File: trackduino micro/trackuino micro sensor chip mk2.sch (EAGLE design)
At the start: 39 parts, among them IC2 74AHC1G125DBV, SW1 SPST_TACT-KMR2, U1 ATMEGA168MLF, Y1 16MHZ

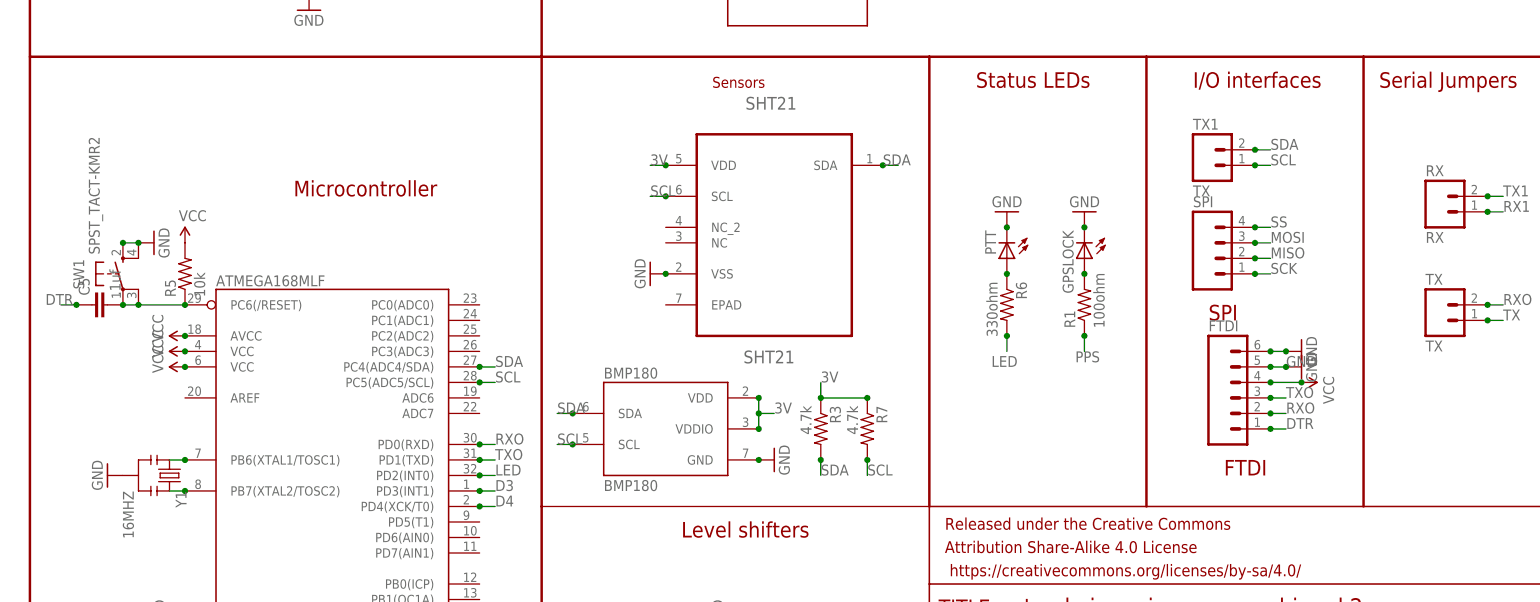
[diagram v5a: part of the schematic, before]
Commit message: Removed Reset Switch
removed reset switch from chip version and added a separate reset line
for ICSP / FTDI programming
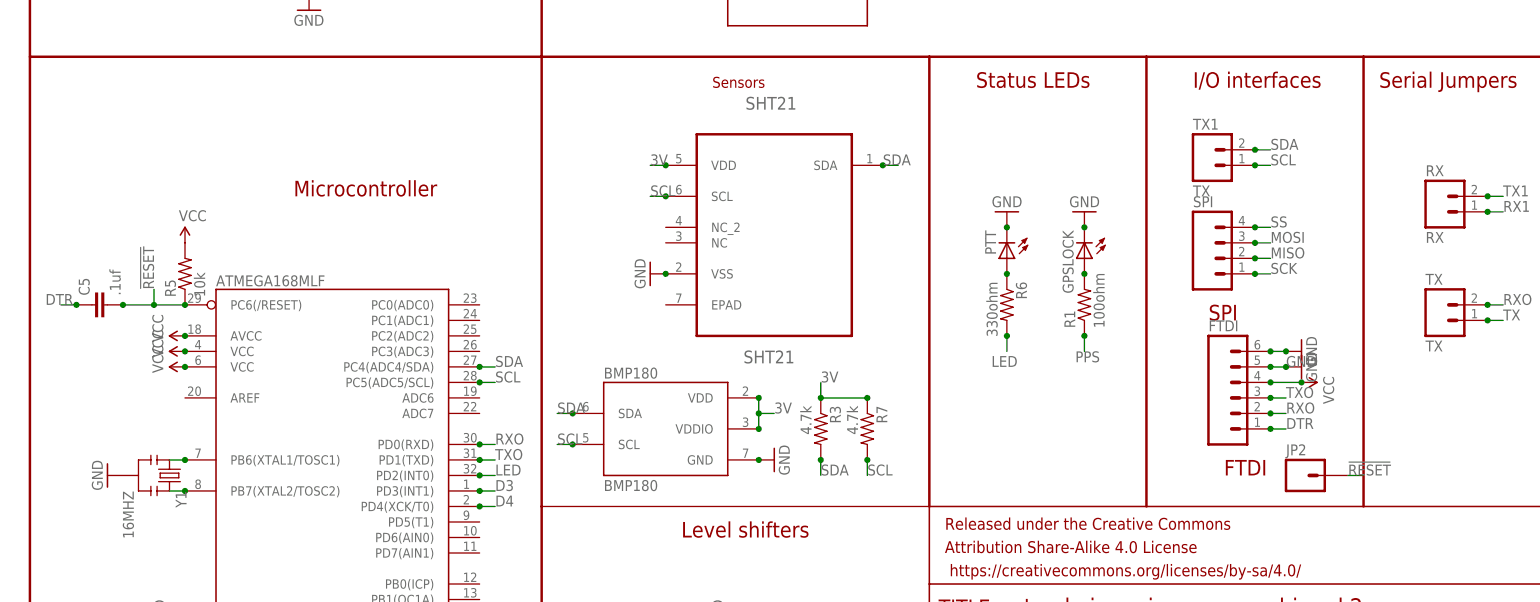
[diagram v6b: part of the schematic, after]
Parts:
- removed SW1: SPST_TACT-KMR2, adafruit:SPST_TACT-KMR2
- added JP2: (no value), SparkFun-Connectors:M01PTH
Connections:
- removed net N$17: C5.2, R5.1, SW1.P, SW1.P1, U1.PC6(/RESET)
- new net !RESET: C5.2, JP2.1, R5.1, U1.PC6(/RESET)
- net GND: no longer SW1.S, SW1.S1
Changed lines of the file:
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@@
 <?xml version="1.0" encoding="utf-8"?>
 <!DOCTYPE eagle SYSTEM "eagle.dtd">
-<eagle version="7.1.0">
+<eagle version="7.3.0">
 <drawing>
 <settings>
@@
 <layer number="56" name="wert" color="7" fill="1" visible="no" active="no"/>
 <layer number="57" name="tCAD" color="7" fill="1" visible="no" active="no"/>
+<layer number="59" name="tCarbon" color="7" fill="1" visible="no" active="no"/>
+<layer number="60" name="bCarbon" color="7" fill="1" visible="no" active="no"/>
 <layer number="90" name="Modules" color="5" fill="1" visible="yes" active="yes"/>
 <layer number="91" name="Nets" color="2" fill="1" visible="yes" active="yes"/>
@@
 <layer number="113" name="IDFDebug" color="7" fill="1" visible="yes" active="yes"/>
 <layer number="116" name="Patch_BOT" color="9" fill="4" visible="yes" active="yes"/>
+<layer number="118" name="Rect_Pads" color="7" fill="1" visible="yes" active="yes"/>
 <layer number="121" name="_tsilk" color="7" fill="1" visible="yes" active="yes"/>
 <layer number="122" name="_bsilk" color="7" fill="1" visible="yes" active="yes"/>
@@
 <layer number="127" name="_tValues" color="7" fill="1" visible="yes" active="yes"/>
 <layer number="128" name="_bValues" color="7" fill="1" visible="yes" active="yes"/>
+<layer number="129" name="Mask" color="7" fill="1" visible="yes" active="yes"/>
 <layer number="131" name="tAdjust" color="7" fill="1" visible="yes" active="yes"/>
 <layer number="132" name="bAdjust" color="7" fill="1" visible="yes" active="yes"/>
@@
 <layer number="223" name="223bmp" color="24" fill="1" visible="no" active="no"/>
 <layer number="224" name="224bmp" color="25" fill="1" visible="no" active="no"/>
+<layer number="225" name="225bmp" color="7" fill="1" visible="yes" active="yes"/>
+<layer number="226" name="226bmp" color="7" fill="1" visible="yes" active="yes"/>
+<layer number="227" name="227bmp" color="7" fill="1" visible="yes" active="yes"/>
+<layer number="228" name="228bmp" color="7" fill="1" visible="yes" active="yes"/>
+<layer number="229" name="229bmp" color="7" fill="1" visible="yes" active="yes"/>
+<layer number="230" name="230bmp" color="7" fill="1" visible="yes" active="yes"/>
+<layer number="231" name="231bmp" color="7" fill="1" visible="yes" active="yes"/>
 <layer number="248" name="Housing" color="7" fill="1" visible="yes" active="yes"/>
 <layer number="249" name="Edge" color="7" fill="1" visible="yes" active="yes"/>
@@
 <layer number="251" name="SMDround" color="12" fill="11" visible="no" active="no"/>
 <layer number="254" name="cooling" color="7" fill="1" visible="yes" active="yes"/>
+<layer number="255" name="routoute" color="7" fill="1" visible="yes" active="yes"/>
 </layers>
 <schematic xreflabel="%F%N/%S.%C%R" xrefpart="/%S.%C%R">
@@
 <part name="TX" library="SparkFun-Connectors" deviceset="M02" device="JST-PTH-VERT" value="TX"/>
 <part name="SPI" library="SparkFun-Connectors" deviceset="M04" device="JST-PTH-VERT"/>
-<part name="GND23" library="SparkFun-Aesthetics" deviceset="GND" device=""/>
 <part name="FRAME1" library="SparkFun-Aesthetics" deviceset="FRAME-LETTER" device=""/>
 <part name="SUPPLY11" library="SparkFun-Aesthetics" deviceset="VCC" device=""/>
@@
 <part name="Y1" library="SparkFun-FreqCtrl" deviceset="RESONATOR" device="16MHZ" value="16MHZ"/>
 <part name="U$1" library="Ava" deviceset="UBLOX_MAX" device=""/>
-<part name="SW1" library="adafruit" deviceset="SPST_TACT" device="-KMR2"/>
 <part name="GND1" library="SparkFun-Aesthetics" deviceset="GND" device=""/>
 <part name="GND3" library="SparkFun-Aesthetics" deviceset="GND" device=""/>
@@
 <part name="U$3" library="SparkFun-RF" deviceset="ANTENNA2" device="SMD3"/>
 <part name="TX1" library="SparkFun-Connectors" deviceset="M02" device="JST-PTH-VERT" value="TX"/>
+<part name="JP2" library="SparkFun-Connectors" deviceset="M01" device="PTH"/>
 </parts>
 <sheets>
@@
 <instance part="TX" gate="G$1" x="231.14" y="66.04"/>
 <instance part="SPI" gate="G$1" x="195.58" y="76.2"/>
-<instance part="GND23" gate="1" x="20.32" y="78.74" rot="R90"/>
 <instance part="FRAME1" gate="G$1" x="0" y="0"/>
 <instance part="FRAME1" gate="G$2" x="147.32" y="0"/>
@@
 <instance part="Y1" gate="G$1" x="22.86" y="40.64" rot="R270"/>
 <instance part="U$1" gate="G$1" x="198.12" y="154.94"/>
-<instance part="SW1" gate="G$1" x="15.24" y="73.66"/>
 <instance part="GND1" gate="1" x="66.04" y="167.64" rot="R90"/>
 <instance part="GND3" gate="1" x="17.78" y="157.48"/>
@@
 <instance part="U$3" gate="G$1" x="165.1" y="165.1" rot="R90"/>
 <instance part="TX1" gate="G$1" x="193.04" y="91.44"/>
+<instance part="JP2" gate="G$1" x="208.28" y="40.64"/>
 </instances>
 <busses>
@@
 </segment>
 <segment>
-<pinref part="GND23" gate="1" pin="GND"/>
-<wire x1="15.24" y1="78.74" x2="17.78" y2="78.74" width="0.1524" layer="91"/>
-<pinref part="SW1" gate="G$1" pin="S"/>
-<pinref part="SW1" gate="G$1" pin="S1"/>
-<junction x="17.78" y="78.74"/>
-<junction x="15.24" y="78.74"/>
-</segment>
-<segment>
 <pinref part="U1" gate="G$1" pin="AGND"/>
 <pinref part="GND25" gate="1" pin="GND"/>
@@
 </segment>
 </net>
-<net name="N$17" class="0">
-<segment>
-<pinref part="C5" gate="G$1" pin="2"/>
-<pinref part="C5" gate="G$1" pin="2"/>
-<pinref part="SW1" gate="G$1" pin="P1"/>
-<wire x1="15.24" y1="68.58" x2="17.78" y2="68.58" width="0.1524" layer="91"/>
-<pinref part="U1" gate="G$1" pin="PC6(/RESET)"/>
-<pinref part="R5" gate="G$1" pin="1"/>
-<wire x1="17.78" y1="68.58" x2="25.4" y2="68.58" width="0.1524" layer="91"/>
-<pinref part="SW1" gate="G$1" pin="P"/>
-<junction x="15.24" y="68.58"/>
-<junction x="17.78" y="68.58"/>
-<junction x="25.4" y="68.58"/>
-</segment>
-</net>
 <net name="RX1" class="0">
 <segment>
@@
 </segment>
 </net>
+<net name="!RESET" class="0">
+<segment>
+<pinref part="JP2" gate="G$1" pin="1"/>
+<wire x1="215.9" y1="40.64" x2="218.44" y2="40.64" width="0.1524" layer="91"/>
+<label x="215.9" y="40.64" size="1.778" layer="95"/>
+</segment>
+<segment>
+<pinref part="C5" gate="G$1" pin="2"/>
+<pinref part="C5" gate="G$1" pin="2"/>
+<pinref part="U1" gate="G$1" pin="PC6(/RESET)"/>
+<pinref part="R5" gate="G$1" pin="1"/>
+<wire x1="15.24" y1="68.58" x2="20.32" y2="68.58" width="0.1524" layer="91"/>
+<junction x="15.24" y="68.58"/>
+<junction x="25.4" y="68.58"/>
+<wire x1="20.32" y1="68.58" x2="25.4" y2="68.58" width="0.1524" layer="91"/>
+<wire x1="20.32" y1="68.58" x2="20.32" y2="71.12" width="0.1524" layer="91"/>
+<label x="20.32" y="71.12" size="1.778" layer="95" rot="R90"/>
+<junction x="20.32" y="68.58"/>
+</segment>
+</net>

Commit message: FTDI Fix
Rewired micro chip ftdi header so RX / TX were broken out correctly.
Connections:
- net RXO: now also FTDI.3; no longer FTDI.2
- net TXO: now also FTDI.2; no longer FTDI.3
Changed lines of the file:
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@@
-</segment>
-<segment>
-<pinref part="FTDI" gate="G$1" pin="2"/>
-<wire x1="203.2" y1="50.8" x2="205.74" y2="50.8" width="0.1524" layer="91"/>
-<label x="205.74" y="50.8" size="1.778" layer="95"/>
-<junction x="203.2" y="50.8"/>
 </segment>
 <segment>
@@
 <label x="241.3" y="68.58" size="1.778" layer="95"/>
 <junction x="238.76" y="68.58"/>
+</segment>
+<segment>
+<pinref part="FTDI" gate="G$1" pin="3"/>
+<wire x1="203.2" y1="53.34" x2="205.74" y2="53.34" width="0.1524" layer="91"/>
+<label x="205.74" y="53.34" size="1.778" layer="95"/>
+<junction x="203.2" y="53.34"/>
 </segment>
 </net>
@@
 </segment>
 <segment>
-<pinref part="FTDI" gate="G$1" pin="3"/>
-<wire x1="203.2" y1="53.34" x2="205.74" y2="53.34" width="0.1524" layer="91"/>
-<label x="205.74" y="53.34" size="1.778" layer="95"/>
-<junction x="203.2" y="53.34"/>
-</segment>
-<segment>
 <pinref part="IC2" gate="A" pin="I"/>
 <wire x1="106.68" y1="7.62" x2="104.14" y2="7.62" width="0.1524" layer="91"/>
@@
 <junction x="106.68" y="7.62"/>
 </segment>
+<segment>
+<pinref part="FTDI" gate="G$1" pin="2"/>
+<wire x1="203.2" y1="50.8" x2="205.74" y2="50.8" width="0.1524" layer="91"/>
+<label x="205.74" y="50.8" size="1.778" layer="95"/>
+<junction x="203.2" y="50.8"/>
+</segment>
 </net>
